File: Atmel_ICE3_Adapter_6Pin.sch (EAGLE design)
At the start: 2 parts

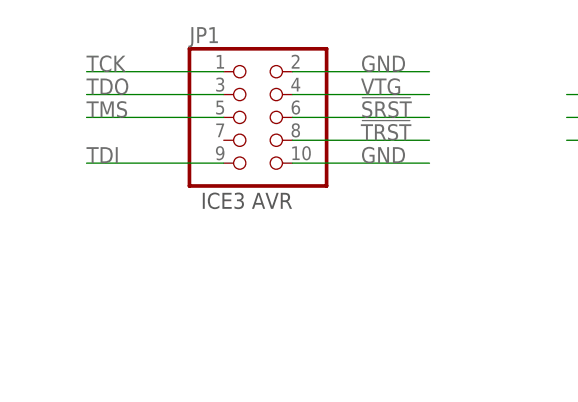
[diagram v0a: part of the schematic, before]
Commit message: Fix 6 pin wrong ICE3 header
Add 10 pin
Add gerber files
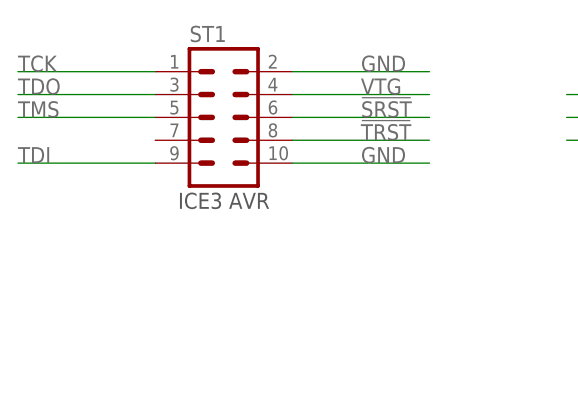
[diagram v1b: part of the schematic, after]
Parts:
- removed JP1: (no value), pinhead_2:PINHD-2X5_2.00
- added ST1: MA05-2_WANNE, pin-header-1.27:MA05-2_WANNE
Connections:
- net !SRST: now also ST1.6; no longer JP1.6
- net !TRST: now also ST1.8; no longer JP1.8
- net GND: now also ST1.10, ST1.2; no longer JP1.10, JP1.2
- net TCK: now also ST1.1; no longer JP1.1
- net TDI: now also ST1.9; no longer JP1.9
- net TDO: now also ST1.3; no longer JP1.3
- net TMS: now also ST1.5; no longer JP1.5
- net VTG: now also ST1.4; no longer JP1.4
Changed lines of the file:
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@@
 <parts>
 <part name="FRAME1" library="frames" deviceset="DINA4_L" device=""/>
-<part name="JP1" library="pinhead_2" deviceset="PINHD-2X5" device="_2.00"/>
 <part name="JP2" library="pinhead_2" deviceset="PINHD-2X3" device="_2.54"/>
+<part name="ST1" library="pin-header-1.27" deviceset="MA05-2_WANNE" device=""/>
 </parts>
 <sheets>
 <sheet>
 <plain>
-<text x="96.52" y="96.52" size="1.778" layer="97">ICE3 AVR</text>
+<text x="93.98" y="96.52" size="1.778" layer="97">ICE3 AVR</text>
 <text x="152.4" y="99.06" size="1.778" layer="97">ISP AVR</text>
 <text x="179.324" y="26.416" size="5.08" layer="97">Adapter ICE3 AVR</text>
@@
 <instance part="FRAME1" gate="G$1" x="0" y="0"/>
 <instance part="FRAME1" gate="G$2" x="162.56" y="0"/>
-<instance part="JP1" gate="A" x="101.6" y="106.68"/>
 <instance part="JP2" gate="A" x="154.94" y="106.68"/>
+<instance part="ST1" gate="G$1" x="99.06" y="106.68" smashed="yes" rot="R180">
+<attribute name="NAME" x="95.25" y="115.062" size="1.778" layer="95"/>
+</instance>
 </instances>
 <busses>
@@
 <net name="TCK" class="0">
 <segment>
-<pinref part="JP1" gate="A" pin="1"/>
-<wire x1="99.06" y1="111.76" x2="83.82" y2="111.76" width="0.1524" layer="91"/>
-<label x="83.82" y="111.76" size="1.778" layer="95"/>
+<wire x1="91.44" y1="111.76" x2="76.2" y2="111.76" width="0.1524" layer="91"/>
+<label x="76.2" y="111.76" size="1.778" layer="95"/>
+<pinref part="ST1" gate="G$1" pin="1"/>
 </segment>
 <segment>
@@
 <net name="TDO" class="0">
 <segment>
-<pinref part="JP1" gate="A" pin="3"/>
-<wire x1="99.06" y1="109.22" x2="83.82" y2="109.22" width="0.1524" layer="91"/>
-<label x="83.82" y="109.22" size="1.778" layer="95"/>
+<wire x1="91.44" y1="109.22" x2="76.2" y2="109.22" width="0.1524" layer="91"/>
+<label x="76.2" y="109.22" size="1.778" layer="95"/>
+<pinref part="ST1" gate="G$1" pin="3"/>
 </segment>
 <segment>
@@
 <net name="TMS" class="0">
 <segment>
-<pinref part="JP1" gate="A" pin="5"/>
-<wire x1="99.06" y1="106.68" x2="83.82" y2="106.68" width="0.1524" layer="91"/>
-<label x="83.82" y="106.68" size="1.778" layer="95"/>
+<wire x1="91.44" y1="106.68" x2="76.2" y2="106.68" width="0.1524" layer="91"/>
+<label x="76.2" y="106.68" size="1.778" layer="95"/>
+<pinref part="ST1" gate="G$1" pin="5"/>
 </segment>
 </net>
 <net name="TDI" class="0">
 <segment>
-<pinref part="JP1" gate="A" pin="9"/>
-<wire x1="99.06" y1="101.6" x2="83.82" y2="101.6" width="0.1524" layer="91"/>
-<label x="83.82" y="101.6" size="1.778" layer="95"/>
+<wire x1="91.44" y1="101.6" x2="76.2" y2="101.6" width="0.1524" layer="91"/>
+<label x="76.2" y="101.6" size="1.778" layer="95"/>
+<pinref part="ST1" gate="G$1" pin="9"/>
 </segment>
 <segment>
@@
 <net name="GND" class="0">
 <segment>
-<pinref part="JP1" gate="A" pin="2"/>
 <wire x1="106.68" y1="111.76" x2="121.92" y2="111.76" width="0.1524" layer="91"/>
 <label x="114.3" y="111.76" size="1.778" layer="95"/>
+<pinref part="ST1" gate="G$1" pin="2"/>
 </segment>
 <segment>
-<pinref part="JP1" gate="A" pin="10"/>
 <wire x1="106.68" y1="101.6" x2="121.92" y2="101.6" width="0.1524" layer="91"/>
 <label x="114.3" y="101.6" size="1.778" layer="95"/>
+<pinref part="ST1" gate="G$1" pin="10"/>
 </segment>
 <segment>
@@
 <net name="VTG" class="0">
 <segment>
-<pinref part="JP1" gate="A" pin="4"/>
 <wire x1="106.68" y1="109.22" x2="121.92" y2="109.22" width="0.1524" layer="91"/>
 <label x="114.3" y="109.22" size="1.778" layer="95"/>
+<pinref part="ST1" gate="G$1" pin="4"/>
 </segment>
 <segment>
@@
 <net name="!SRST" class="0">
 <segment>
-<pinref part="JP1" gate="A" pin="6"/>
 <wire x1="106.68" y1="106.68" x2="121.92" y2="106.68" width="0.1524" layer="91"/>
 <label x="114.3" y="106.68" size="1.778" layer="95"/>
+<pinref part="ST1" gate="G$1" pin="6"/>
 </segment>
 <segment>
@@
 <net name="!TRST" class="0">
 <segment>
-<pinref part="JP1" gate="A" pin="8"/>
 <wire x1="106.68" y1="104.14" x2="121.92" y2="104.14" width="0.1524" layer="91"/>
 <label x="114.3" y="104.14" size="1.778" layer="95"/>
+<pinref part="ST1" gate="G$1" pin="8"/>
 </segment>
 </net>
